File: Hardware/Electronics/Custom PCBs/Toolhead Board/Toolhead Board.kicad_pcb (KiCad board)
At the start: 6 copper layers, 75 x 75 mm, 173 parts, among them J1 USB C Receptacle, J10 Conn_01x02, J11 Conn_01x02, J12 120TR, J2 Conn_02x08_Odd_Even, J3 Conn_02x08_Odd_Even, J4 Conn_02x08_Odd_Even, J5 Conn_02x04_Odd_Even, J6 Conn_02x04_Odd_Even, Q1 MMBT4403, Q2 MMBT4403, Q3 MMBT4403, SW1 BOOT, SW2 RESET, U1 LF15_TO220, U10 BMI270, U11 G20N06D52, U12 G20N06D52, U13 PCA9685BS, U2 LF15_TO220, U3 RP2040, U4 W25Q128JVS, U5 SN65HVD1050D, U6 TMC2209-LA, U7 HX711, U8 HX711, U9 HX711, Y1 12MHz/12pF/50Ω/20ppm

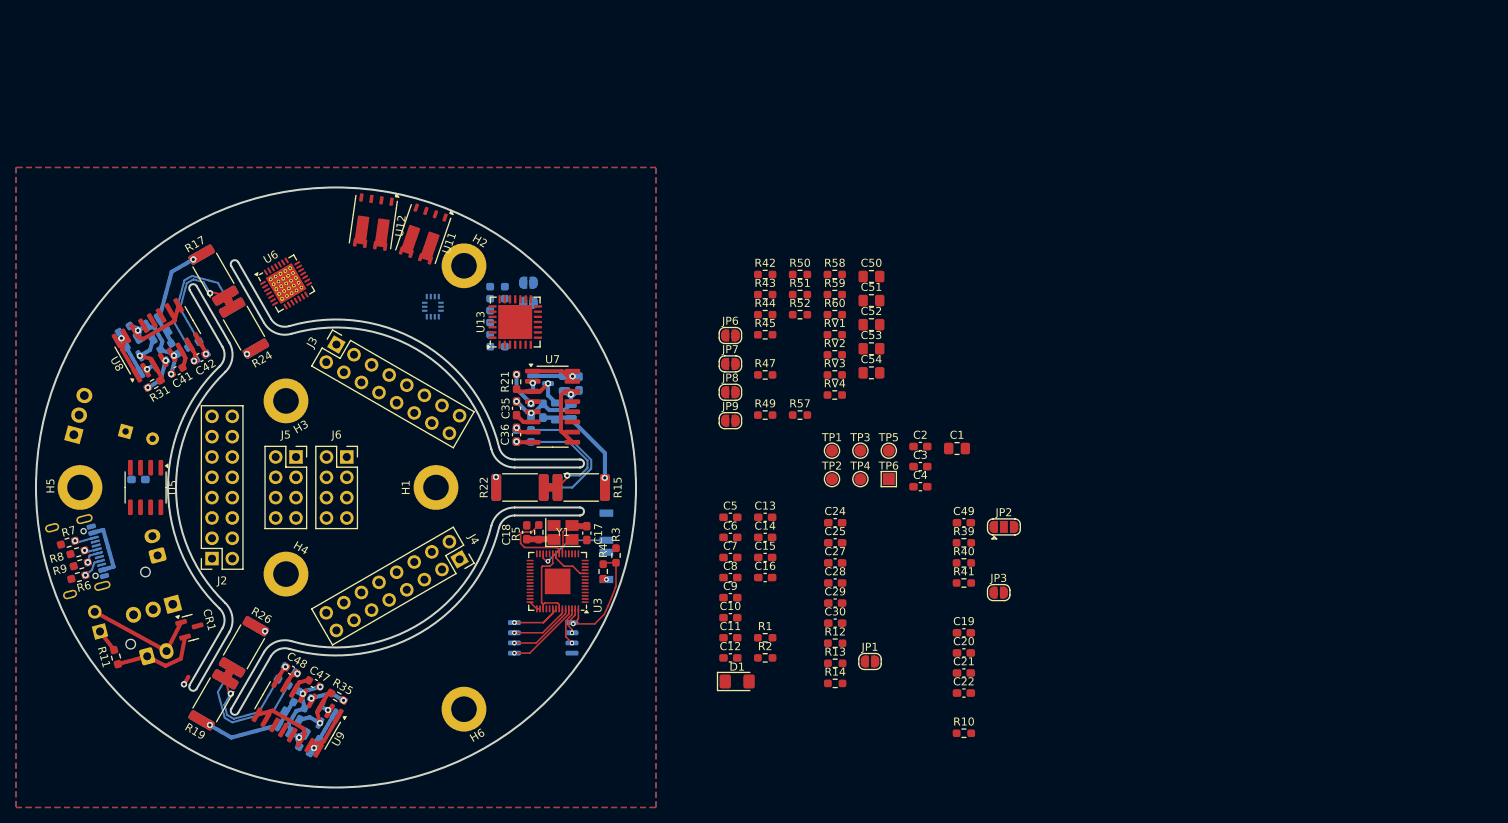
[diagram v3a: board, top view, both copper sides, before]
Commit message: Update toolhead board layout
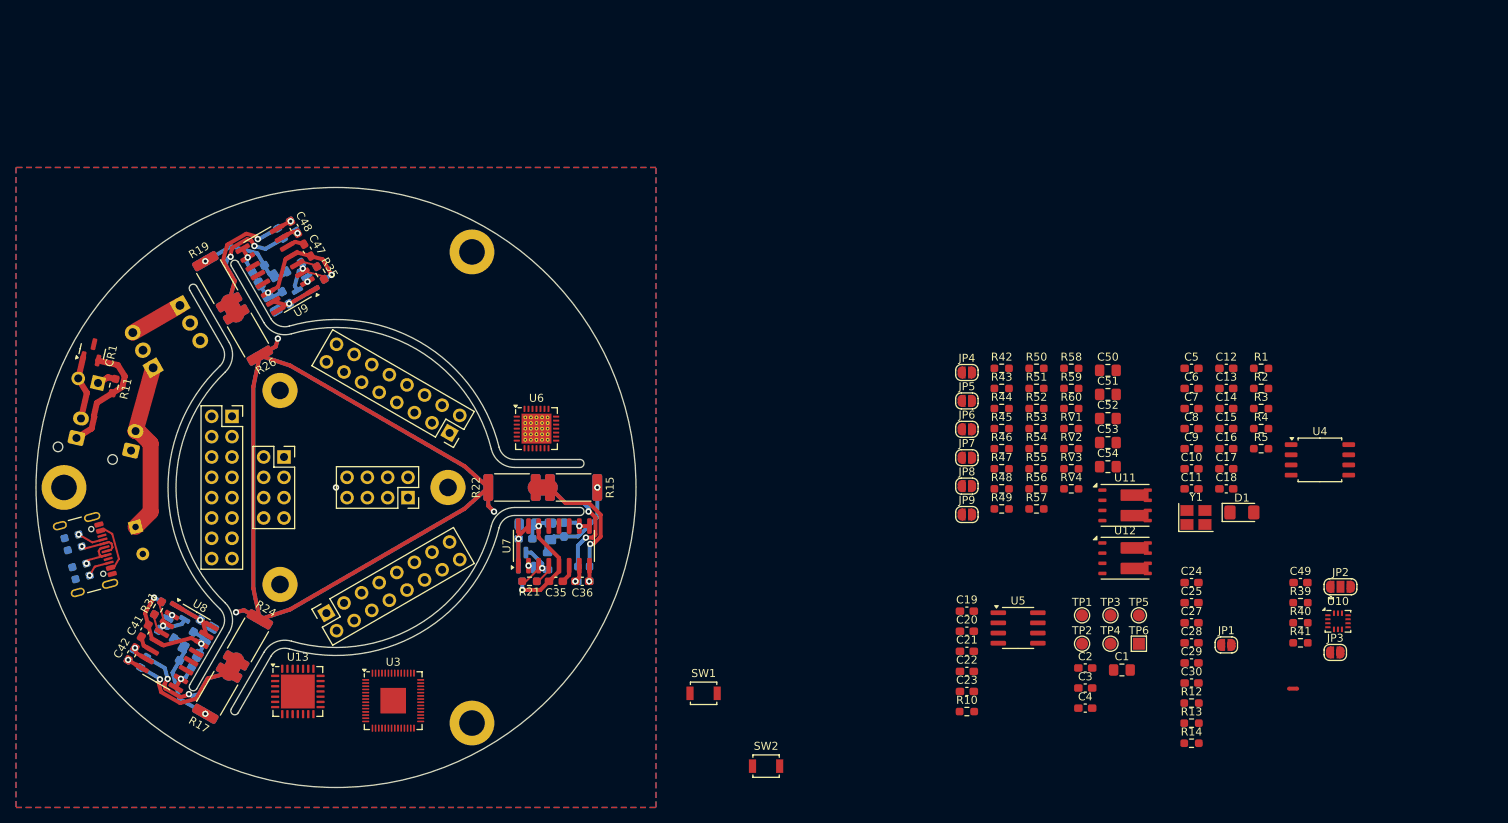
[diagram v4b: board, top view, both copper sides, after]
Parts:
- removed the H1 at (87.5, 75.0)
- removed the H2 at (91.0, 47.3)
- removed H3, H4, H5, H6: MountingHole, MountingHole:MountingHole_3.2mm_M3_DIN965_Pad
- added H1: MountingHole, MountingHole:MountingHole_3.2mm_M3_DIN965_Pad, F.Cu at (41.0, 75.0)
- added H1: MountingHole, MountingHole:MountingHole_3.2mm_M3_DIN965_Pad, F.Cu at (92.0, 104.4)
- added H1: MountingHole, MountingHole:MountingHole_3.2mm_M3_DIN965_Pad, F.Cu at (92.0, 45.6)
- added H2: MountingHole, MountingHole:MountingHole_2.2mm_M2_Pad, F.Cu at (68.0, 87.1)
- added H2: MountingHole, MountingHole:MountingHole_2.2mm_M2_Pad, F.Cu at (68.0, 62.9)
- added H2: MountingHole, MountingHole:MountingHole_2.2mm_M2_Pad, F.Cu at (89.0, 75.0)
- C23, J1, JP4, JP5, R46, R48, R53, R54, R55, R56, SW1, SW2, U10, U4: moved to F.Cu
- C31, C33, C37, C39, C43, C45: footprint Capacitor_SMD:C_0805_2012Metric -> Capacitor_SMD:C_0805_2012Metric_Pad1.18x1.45mm_HandSolder
- C38, C40, C41, C42, C44, C46, C47, C48: footprint Capacitor_SMD:C_0603_1608Metric -> Capacitor_SMD:C_0603_1608Metric_Pad1.08x0.95mm_HandSolder
- R6, R7, R8, R9: moved to B.Cu
- U11, U12: footprint lib:WDFN-8-1EP_6x5mm_P1.27mm_EP3.4x4mm_No_Center_Pad -> Library:WDFN-8-1EP_6x5mm_P1.27mm_EP3.4x4mm_No_Center_Pad
- moved NT1 138.3 mm to (194.6, 100.1), turned to 0 degrees
- moved U10 119.8 mm to (200.2, 91.7), turned to 0 degrees
- moved U5 110.5 mm to (160.3, 92.6), turned to 0 degrees
- moved C23 106.9 mm to (153.9, 100.5)
- moved U12 102.9 mm to (173.6, 83.8), turned to 0 degrees
- moved U4 99.6 mm to (198.0, 71.5), turned to 0 degrees
- moved U11 94.1 mm to (173.6, 77.2), turned to 0 degrees
- moved R5 90.9 mm to (190.6, 70.2), turned to 0 degrees
- moved C18 87.6 mm to (186.3, 75.2), turned to 0 degrees
- moved R4 84.2 mm to (190.6, 67.6), turned to 0 degrees
- moved R3 82.7 mm to (190.6, 65.1), turned to 0 degrees
- moved C17 80.3 mm to (186.3, 72.7), turned to 0 degrees
- moved Y1 79.1 mm to (182.5, 78.8)
- moved C12 71.8 mm to (186.3, 60.1)
- moved R1 70.5 mm to (190.6, 60.1)
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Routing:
- net GNDA: track 189.3 -> 344.0 mm, vias 13 -> 12
- net +5V: track 66.9 -> 6.80 mm
- net V_MOT: track 44.6 -> 21.9 mm
- net /Microcontroller/QSPI_SS: track 14.9 -> 0.00 mm, vias 1 -> 0
- net +3.3V: track 14.7 -> 0.00 mm, vias 1 -> 0
- net +1V1: track 10.8 -> 0.00 mm
- net /Microcontroller/RUN: track 9.68 -> 0.00 mm, vias 1 -> 0
- net Net-(U3-XOUT): track 9.65 -> 0.00 mm
- net /Microcontroller/QSPI_SD0: track 9.48 -> 0.00 mm, vias 1 -> 0
- net /Microcontroller/QSPI_SCK: track 8.51 -> 0.00 mm, vias 1 -> 0
- net /Microcontroller/QSPI_SD3: track 7.55 -> 0.00 mm, vias 1 -> 0
- net Net-(U3-XIN): track 6.14 -> 0.00 mm
- net /CAN IO/CAN_H: track 14.3 -> 8.15 mm
- net /Microcontroller/QSPI_SD2: track 4.90 -> 0.00 mm, vias 1 -> 0
- net Net-(J1-D--PadA7): track 1.63 -> 5.41 mm
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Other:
- copper layers 6 -> 4
- board text removed: "BOOT"
- board text removed: "CAN"
- board text removed: "PWR"
- board text removed: "RST"

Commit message: Update toolhead layout
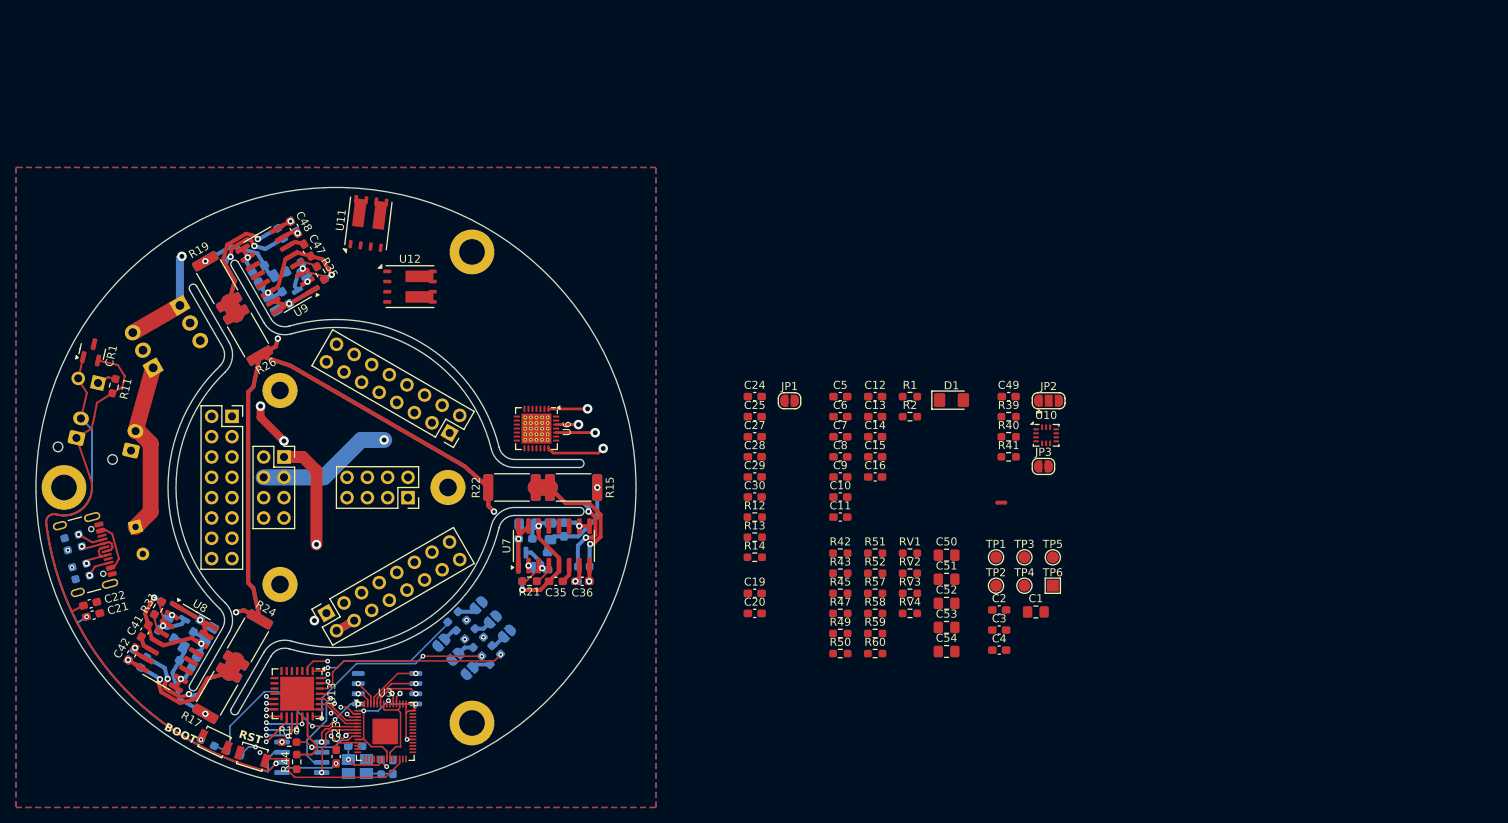
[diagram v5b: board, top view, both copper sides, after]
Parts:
- C17, C18, JP4, JP5, JP6, JP7, JP8, JP9, R3, R4, R46, R48, R5, R53, R54, R55, R56, U4, U5, Y1: moved to B.Cu
- moved R4 137.4 mm to (59.0, 106.9), turned to -25.5 degrees
- moved R3 135.5 mm to (62.2, 108.2), turned to -17.25 degrees
- moved U4 120.1 mm to (81.4, 100.2)
- moved R5 117.0 mm to (80.6, 109.9), turned to 90 degrees
- moved C17 114.3 mm to (77.4, 107.3), turned to 180 degrees
- moved C22 109.9 mm to (44.3, 89.5), turned to 15 degrees
- moved C18 109.8 mm to (82.1, 109.9), turned to -90 degrees
- moved Y1 109.3 mm to (77.7, 109.9), turned to 180 degrees
- moved C21 109.3 mm to (44.6, 91.0), turned to 15 degrees
- moved U11 100.9 mm to (79.1, 42.0), turned to 83 degrees
- moved R44 98.6 mm to (70.1, 109.3), turned to 90 degrees
- moved U12 95.6 mm to (84.2, 49.9)
- moved U5 91.0 mm to (70.7, 108.7), turned to 180 degrees
- moved R10 84.8 mm to (69.2, 106.8)
- moved C23 79.3 mm to (75.0, 108.6), turned to 90 degrees
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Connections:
- J2 pad 10: D15 -> GND
- J2 pad 11: D9 -> GND
- J2 pad 12: D16 -> GND
- J2 pad 13: D10 -> GND
- J2 pad 14: D11 -> GND
- J2 pad 4: /Microcontroller/LED -> D7
- J2 pad 6: D12 -> D8
- J2 pad 7: D7 -> SDA
- J2 pad 8: D14 -> SCL
- J2 pad 9: D8 -> GND
- J3 pad 11: SDA -> GND
- J3 pad 12: SCL -> GND
- J6 pad 5: unconnected-(J6-Pin_5-Pad5) -> GND
- J6 pad 6: unconnected-(J6-Pin_6-Pad6) -> GND
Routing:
- net +3.3V: track 0.00 -> 100.0 mm, vias 0 -> 8
- net V_MOT: track 21.9 -> 114.7 mm, vias 0 -> 1
- net +5V: track 6.80 -> 94.1 mm, vias 0 -> 2
- net GNDA: track 344.0 -> 278.8 mm
- net SERVO8: track 0.00 -> 34.8 mm, vias 0 -> 2
- net SERVO7: track 0.00 -> 33.6 mm, vias 0 -> 2
- net SERVO4: track 0.00 -> 32.6 mm, vias 0 -> 1
- net SDA: track 0.00 -> 29.2 mm, vias 0 -> 2
- net SERVO3: track 0.00 -> 28.3 mm, vias 0 -> 1
- net OB2: track 0.00 -> 27.1 mm, vias 0 -> 1
- net /Microcontroller/QSPI_SS: track 0.00 -> 26.4 mm, vias 0 -> 3
- net OA1: track 0.00 -> 26.0 mm, vias 0 -> 1
- net Net-(U13-A5): track 0.00 -> 25.9 mm, vias 0 -> 3
- net Net-(U13-A2): track 0.00 -> 25.7 mm, vias 0 -> 2
- net SCL: track 0.00 -> 25.2 mm, vias 0 -> 1
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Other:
- board text added: "BOOT"
- board text added: "RST"

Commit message: Update layout
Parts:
- JP4, JP5, JP6, JP7, JP8, JP9, R3, R4, R46, R48, R53, R54, R55, R56, U5: moved to F.Cu
- moved R44 97.7 mm to (154.2, 59.7), turned to 0 degrees
- moved D1 90.2 mm to (74.3, 110.0), turned to 180 degrees
- moved R2 87.1 mm to (71.1, 109.3), turned to 90 degrees
- moved R10 83.0 mm to (149.9, 87.5)
- moved C23 78.5 mm to (149.9, 85.0), turned to 0 degrees
- moved U10 75.1 mm to (92.7, 92.7), turned to -135 degrees
- moved R53 74.2 mm to (158.6, 62.2), turned to 0 degrees
- moved R54 73.9 mm to (158.6, 64.7), turned to 0 degrees
- moved JP4 72.2 mm to (149.9, 55.2), turned to 0 degrees
- moved R55 71.7 mm to (158.6, 67.2), turned to 0 degrees
- moved JP5 70.7 mm to (149.9, 58.8), turned to 0 degrees
- moved R56 69.6 mm to (158.6, 69.8), turned to 0 degrees
- moved JP6 69.6 mm to (149.9, 62.3), turned to 0 degrees
- moved R46 67.3 mm to (154.2, 64.7), turned to 0 degrees
- moved R48 66.2 mm to (154.2, 69.8), turned to 0 degrees
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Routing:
- net V_MOT: track 114.7 -> 21.9 mm, vias 1 -> 0
- net +5V: track 94.1 -> 5.08 mm, vias 2 -> 0
- net +3.3V: track 100.0 -> 11.2 mm, vias 8 -> 3
- net SERVO8: track 34.8 -> 0.00 mm, vias 2 -> 0
- net SERVO7: track 33.6 -> 0.00 mm, vias 2 -> 0
- net SERVO4: track 32.6 -> 0.00 mm, vias 1 -> 0
- net SDA: track 29.2 -> 0.00 mm, vias 2 -> 0
- net SERVO3: track 28.3 -> 0.00 mm, vias 1 -> 0
- net OB2: track 27.1 -> 0.00 mm, vias 1 -> 0
- net OA1: track 26.0 -> 0.00 mm, vias 1 -> 0
- net Net-(U13-A5): track 25.9 -> 0.00 mm, vias 3 -> 0
- net Net-(U13-A2): track 25.7 -> 0.00 mm, vias 2 -> 0
- net /Microcontroller/QSPI_SS: track 26.4 -> 0.98 mm, vias 3 -> 1
- net SCL: track 25.2 -> 0.00 mm, vias 1 -> 0
- net Net-(U13-A0): track 25.2 -> 0.00 mm, vias 1 -> 0
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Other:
- board text removed: "BOOT"
- board text removed: "RST"

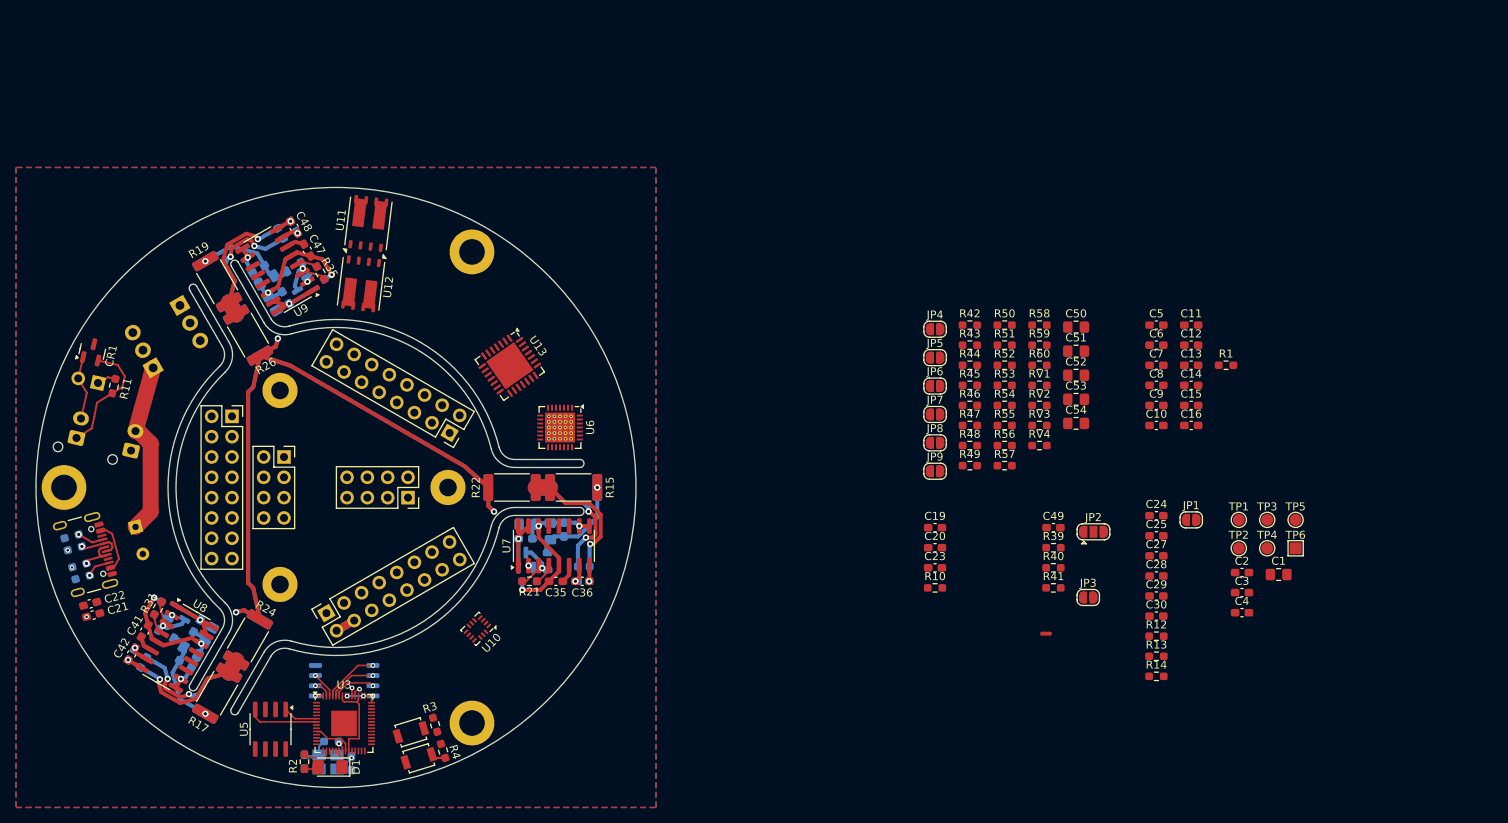
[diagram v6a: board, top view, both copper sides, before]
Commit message: Toolhead Board Updated Traces
Updated Traces, about half of the resistors are done and a few capacitors along with most mp components
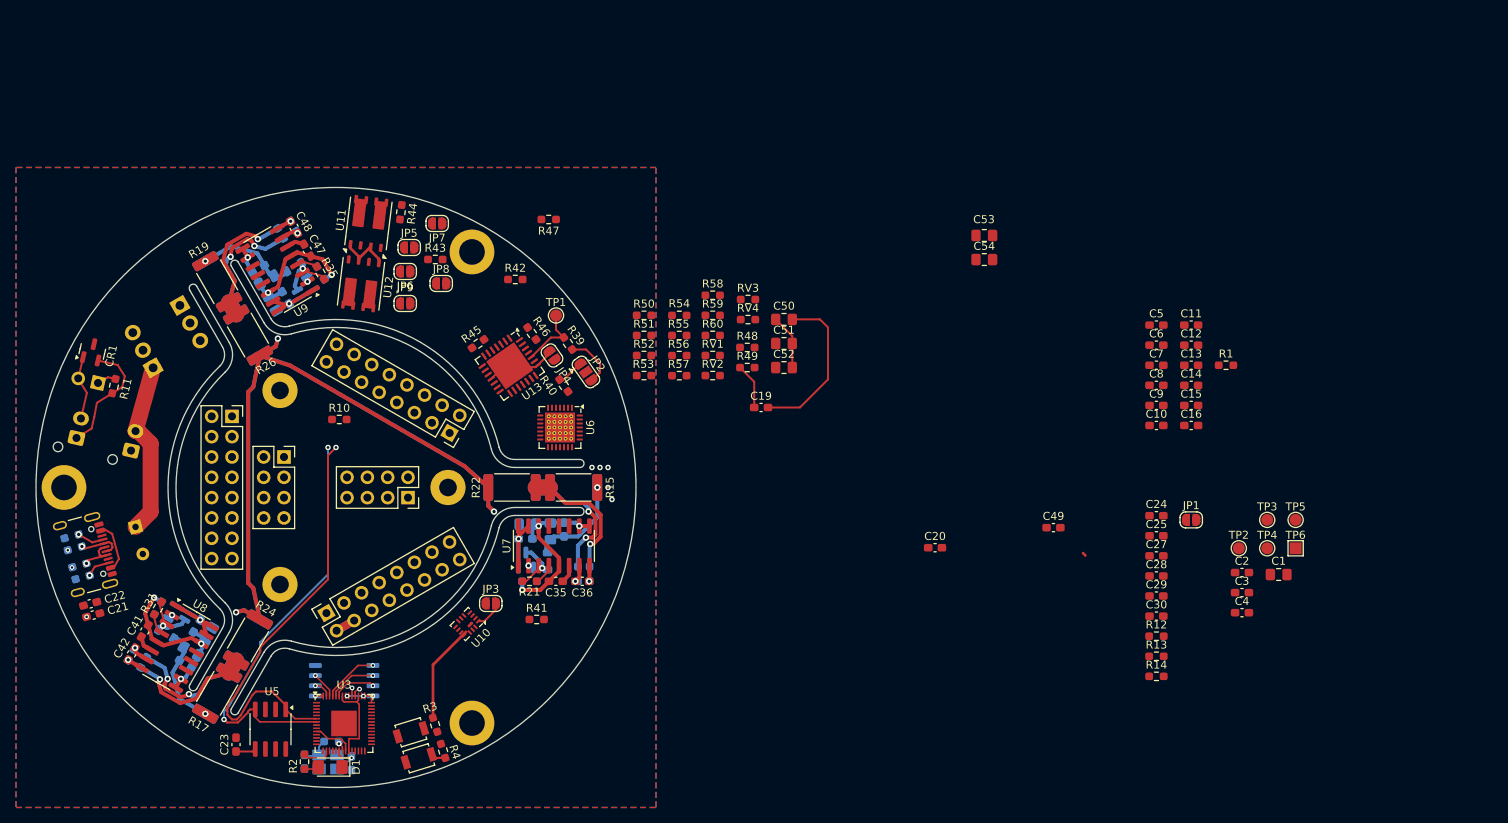
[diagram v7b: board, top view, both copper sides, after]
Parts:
- removed NT1: NetTie_2, NetTie:NetTie-2_SMD_Pad0.5mm
- moved C23 90.1 mm to (62.5, 107.1), turned to 90 degrees
- moved TP1 89.1 mm to (102.5, 53.5)
- moved R10 77.4 mm to (75.4, 66.5)
- moved JP3 74.7 mm to (94.3, 89.5)
- moved R44 73.6 mm to (83.1, 40.6), turned to -97 degrees
- moved JP9 69.5 mm to (83.7, 52.0)
- moved JP6 67.8 mm to (83.7, 48.0), turned to 180 degrees
- moved R43 67.7 mm to (87.4, 46.5)
- moved JP5 67.2 mm to (84.2, 45.0)
- moved JP7 66.7 mm to (87.7, 42.0), turned to 180 degrees
- moved JP2 66.5 mm to (106.2, 60.6), turned to -55 degrees
- moved R39 65.8 mm to (104.0, 57.0), turned to 125 degrees
- moved R40 65.3 mm to (103.5, 62.3), turned to -55 degrees
- moved JP8 64.9 mm to (88.2, 49.5)
- moved R41 64.7 mm to (100.1, 91.5)
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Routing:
- net (no net): track 0.00 -> 85.6 mm, vias 0 -> 5
- net +5V: track 5.08 -> 71.6 mm
- net CAN_TX: track 4.32 -> 65.1 mm, vias 0 -> 1
- net CAN_RX: track 8.87 -> 63.6 mm, vias 0 -> 2
- net GND: track 0.00 -> 30.4 mm
- net SERVO8: track 0.00 -> 23.8 mm
- net SERVO7: track 0.00 -> 21.9 mm
- net SERVO6: track 0.00 -> 19.1 mm
- net SERVO5: track 0.00 -> 16.7 mm
- net +3.3V: track 11.2 -> 23.6 mm
- net SDA: track 0.00 -> 8.22 mm
- net Net-(JP2-B): track 0.00 -> 6.75 mm
- net Net-(JP2-A): track 0.00 -> 3.79 mm
- net /Accelerometer/Address Selection: track 0.00 -> 3.57 mm
- net Net-(U5-VREF): track 0.00 -> 2.54 mm
